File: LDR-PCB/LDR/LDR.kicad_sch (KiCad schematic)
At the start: 7 parts, among them J1 Conn_01x03_Socket, Q1 NPN, U1 ${SIM.PARAMS}

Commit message: merge
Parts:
- added H1, H2: MountingHole_Pad, MountingHole:MountingHole_2.2mm_M2_ISO14580_Pad, symbol Mechanical:MountingHole_Pad
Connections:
- net GND: now also H1.1, H2.1
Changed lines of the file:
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@@
+    (stroke (width 0) (type default))
+  )
+  (wire (pts (xy 96.52 73.025) (xy 96.52 74.93))
     (stroke (width 0) (type default))
   )
@@
   )
   (wire (pts (xy 150.495 85.09) (xy 151.13 85.09))
+    (stroke (width 0) (type default))
+  )
+  (wire (pts (xy 88.265 73.025) (xy 88.265 74.295))
     (stroke (width 0) (type default))
   )
@@
     )
   )
+  (symbol (lib_id "power:GND") (at 88.265 74.295 0) (unit 1)
+    (in_bom yes) (on_board yes) (dnp no) (fields_autoplaced)
+    (property "Reference" "#PWR010" (at 88.265 80.645 0)
+      (effects (font (size 1.27 1.27)) hide)
+    )
+    (property "Value" "GND" (at 88.265 79.375 0)
+      (effects (font (size 1.27 1.27)) hide)
+    )
+    (property "Footprint" "" (at 88.265 74.295 0)
+      (effects (font (size 1.27 1.27)) hide)
+    )
+    (property "Datasheet" "" (at 88.265 74.295 0)
+      (effects (font (size 1.27 1.27)) hide)
+    )
+    (pin "1")
+    (instances
+      (project "LDR"
+        (path "/2e6b5c95-f01c-4aeb-aaa9-5aa7ab28cad0"
+          (reference "#PWR010") (unit 1)
+        )
+      )
+    )
+  )
   (symbol (lib_id "Device:R") (at 138.43 97.79 90) (unit 1)
     (in_bom yes) (on_board yes) (dnp no) (fields_autoplaced)
@@
       (effects (font (size 1.27 1.27)) hide)
     )
+    (pin "1")
+    (pin "2")
     (pin "3")
-    (pin "2")
-    (pin "1")
+    (pin "4")
     (pin "8")
-    (pin "4")
     (instances
       (project "LDR"
@@
     )
   )
+  (symbol (lib_id "power:GND") (at 96.52 74.93 0) (unit 1)
+    (in_bom yes) (on_board yes) (dnp no) (fields_autoplaced)
+    (property "Reference" "#PWR011" (at 96.52 81.28 0)
+      (effects (font (size 1.27 1.27)) hide)
+    )
+    (property "Value" "GND" (at 96.52 80.01 0)
+      (effects (font (size 1.27 1.27)) hide)
+    )
+    (property "Footprint" "" (at 96.52 74.93 0)
+      (effects (font (size 1.27 1.27)) hide)
+    )
+    (property "Datasheet" "" (at 96.52 74.93 0)
+      (effects (font (size 1.27 1.27)) hide)
+    )
+    (pin "1")
+    (instances
+      (project "LDR"
+        (path "/2e6b5c95-f01c-4aeb-aaa9-5aa7ab28cad0"
+          (reference "#PWR011") (unit 1)
+        )
+      )
+    )
+  )
   (symbol (lib_id "power:GND") (at 151.13 93.98 0) (unit 1)
     (in_bom yes) (on_board yes) (dnp no) (fields_autoplaced)
@@
     )
   )
+  (symbol (lib_id "Mechanical:MountingHole_Pad") (at 96.52 70.485 0) (unit 1)
+    (in_bom yes) (on_board yes) (dnp no) (fields_autoplaced)
+    (property "Reference" "H2" (at 99.695 67.945 0)
+      (effects (font (size 1.27 1.27)) (justify left))
+    )
+    (property "Value" "MountingHole_Pad" (at 99.695 70.485 0)
+      (effects (font (size 1.27 1.27)) (justify left) hide)
+    )
+    (property "Footprint" "MountingHole:MountingHole_2.2mm_M2_ISO14580_Pad" (at 96.52 70.485 0)
+      (effects (font (size 1.27 1.27)) hide)
+    )
+    (property "Datasheet" "~" (at 96.52 70.485 0)
+      (effects (font (size 1.27 1.27)) hide)
+    )
+    (pin "1")
+    (instances
+      (project "LDR"
+        (path "/2e6b5c95-f01c-4aeb-aaa9-5aa7ab28cad0"
+          (reference "H2") (unit 1)
+        )
+      )
+    )
+  )
   (symbol (lib_id "Device:R") (at 151.13 88.9 0) (unit 1)
     (in_bom yes) (on_board yes) (dnp no) (fields_autoplaced)
@@
         )
       )
+    )
+  )
+  (symbol (lib_id "Mechanical:MountingHole_Pad") (at 88.265 70.485 0) (unit 1)
+    (in_bom yes) (on_board yes) (dnp no) (fields_autoplaced)
+    (property "Reference" "H1" (at 91.44 67.945 0)
+      (effects (font (size 1.27 1.27)) (justify left))
+    )
+    (property "Value" "MountingHole_Pad" (at 91.44 70.485 0)
+      (effects (font (size 1.27 1.27)) (justify left) hide)
+    )
+    (property "Footprint" "MountingHole:MountingHole_2.2mm_M2_ISO14580_Pad" (at 88.265 70.485 0)
+      (effects (font (size 1.27 1.27)) hide)
+    )
+    (property "Datasheet" "~" (at 88.265 70.485 0)
+      (effects (font (size 1.27 1.27)) hide)
+    )
+    (pin "1")
+    (instances
+      (project "LDR"
+        (path "/2e6b5c95-f01c-4aeb-aaa9-5aa7ab28cad0"
+          (reference "H1") (unit 1)
+        )
+      )

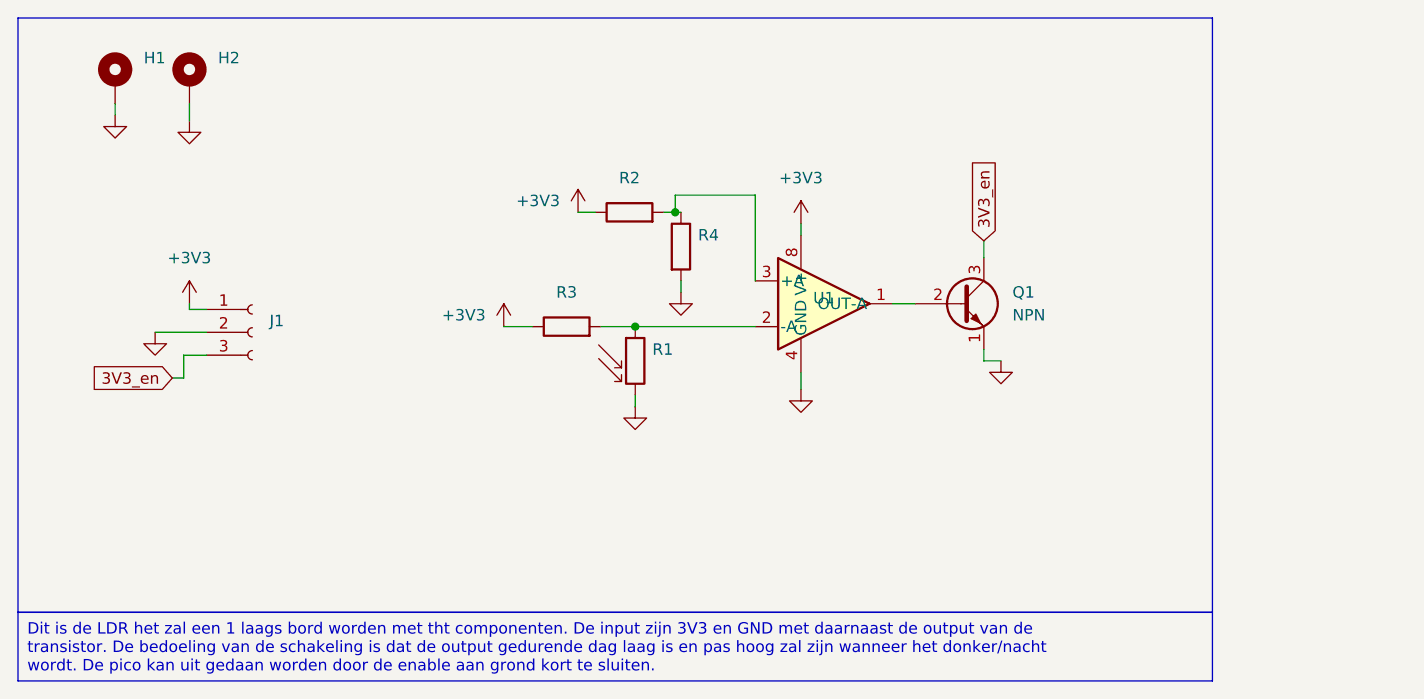
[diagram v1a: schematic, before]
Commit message: LDR schakeling update naar LM311P
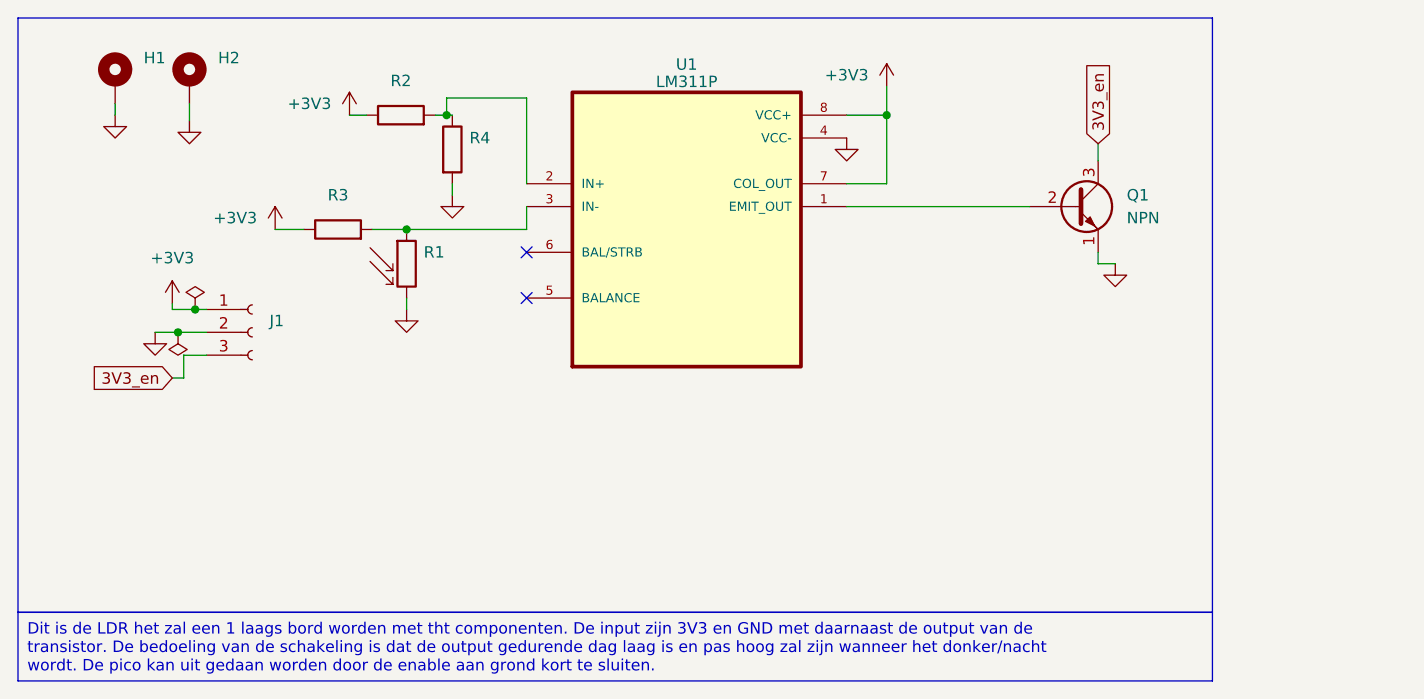
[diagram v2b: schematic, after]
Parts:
- removed U1: ${SIM.PARAMS}, Package_DIP:DIP-8_W7.62mm, symbol Simulation_SPICE:OPAMP
- added U1: LM311P, LM311P:DIP794W45P254L959H508Q8, symbol LM311P:LM311P
- R2, R3: value R -> 2K2
- R4: value R -> 1K8
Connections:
- net +3V3: now also U1.7 (COL_OUT), U1.8 (VCC+)
- net GND: now also U1.4 (VCC-)
- net at R1.1, R3.2: now also U1.3 (IN-)
- net at Q1.2 (B): now also U1.1 (EMIT_OUT)
- net at R2.2, R4.1: now also U1.2 (IN+)
- no-connect marks 0 -> 2
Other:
- moved on the sheet: Q1, R1, R2, R3, R4

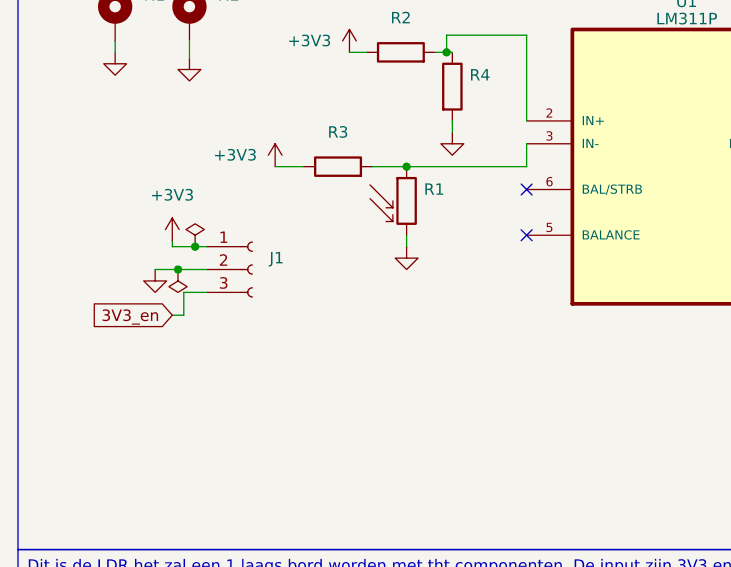
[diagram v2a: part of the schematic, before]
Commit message: LDR connector, silkscreen AC,  Mounting hole main pcb aangepast
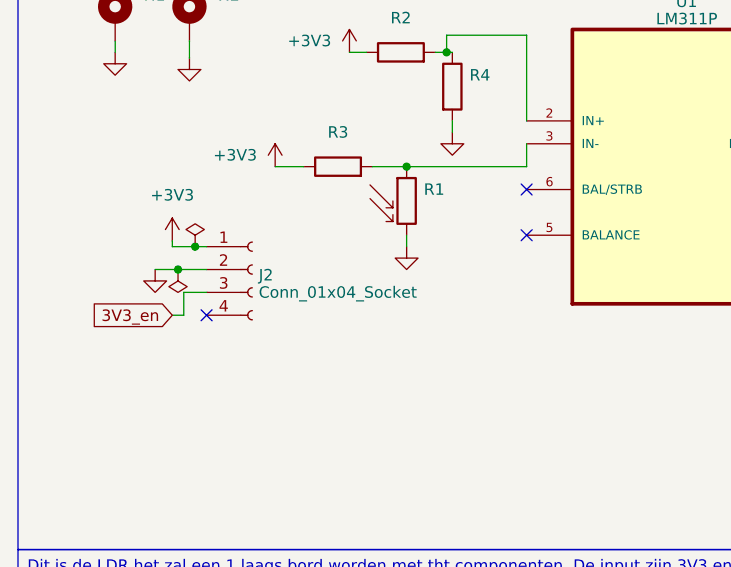
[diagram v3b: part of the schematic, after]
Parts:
- removed J1: Conn_01x03_Socket, Connector_PinSocket_2.00mm:PinSocket_1x03_P2.00mm_Vertical, symbol Connector:Conn_01x03_Socket
- added J2: Conn_01x04_Socket, Connector_JST:JST_EH_B4B-EH-A_1x04_P2.50mm_Vertical, symbol Connector:Conn_01x04_Socket
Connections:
- net +3V3: now also J2.1 (Pin_1)
- net 3V3_en: now also J2.3 (Pin_3)
- net GND: now also J2.2 (Pin_2)
- no-connect marks 2 -> 3
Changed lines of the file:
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@@
   (junction (at 97.155 95.885) (diameter 0) (color 0 0 0 0)
   )
+  (no_connect (at 98.425 103.505))
   (no_connect (at 133.985 89.535))
   (no_connect (at 133.985 94.615))
@@
     )
   )
-  (symbol (lib_id "power:GND") (at 199.39 90.805 0) (unit 1)
-    (in_bom yes) (on_board yes) (dnp no) (fields_autoplaced)
-    (property "Reference" "#PWR07" (at 199.39 97.155 0)
-      (effects (font (size 1.27 1.27)) hide)
-    )
-    (property "Value" "GND" (at 199.39 95.885 0)
-      (effects (font (size 1.27 1.27)) hide)
-    )
-    (property "Footprint" "" (at 199.39 90.805 0)
-      (effects (font (size 1.27 1.27)) hide)
-    )
-    (property "Datasheet" "" (at 199.39 90.805 0)
-      (effects (font (size 1.27 1.27)) hide)
-    )
-    (pin "1")
-    (instances
-      (project "LDR"
-        (path "/2e6b5c95-f01c-4aeb-aaa9-5aa7ab28cad0"
-          (reference "#PWR07") (unit 1)
-        )
-      )
-    )
-  )
-  (symbol (lib_id "Connector:Conn_01x03_Socket") (at 103.505 98.425 0) (unit 1)
-    (in_bom yes) (on_board yes) (dnp no) (fields_autoplaced)
-    (property "Reference" "J1" (at 105.41 97.155 0)
+  (symbol (lib_id "Connector:Conn_01x04_Socket") (at 103.505 98.425 0) (unit 1)
+    (in_bom yes) (on_board yes) (dnp no) (fields_autoplaced)
+    (property "Reference" "J2" (at 104.2162 99.0513 0)
       (effects (font (size 1.27 1.27)) (justify left))
     )
-    (property "Value" "Conn_01x03_Socket" (at 105.41 99.695 0)
-      (effects (font (size 1.27 1.27)) (justify left) hide)
-    )
-    (property "Footprint" "Connector_PinSocket_2.00mm:PinSocket_1x03_P2.00mm_Vertical" (at 103.505 98.425 0)
+    (property "Value" "Conn_01x04_Socket" (at 104.2162 100.9723 0)
+      (effects (font (size 1.27 1.27)) (justify left))
+    )
+    (property "Footprint" "Connector_JST:JST_EH_B4B-EH-A_1x04_P2.50mm_Vertical" (at 103.505 98.425 0)
       (effects (font (size 1.27 1.27)) hide)
     )
@@
     (pin "2")
     (pin "3")
-    (instances
-      (project "LDR"
-        (path "/2e6b5c95-f01c-4aeb-aaa9-5aa7ab28cad0"
-          (reference "J1") (unit 1)
-        )
-      )
+    (pin "4")
+    (instances
+      (project "LDR"
+        (path "/2e6b5c95-f01c-4aeb-aaa9-5aa7ab28cad0"
+          (reference "J2") (unit 1)
+        )
+      )
+    )
+  )
+  (symbol (lib_id "power:GND") (at 199.39 90.805 0) (unit 1)
+    (in_bom yes) (on_board yes) (dnp no) (fields_autoplaced)
+    (property "Reference" "#PWR07" (at 199.39 97.155 0)
+      (effects (font (size 1.27 1.27)) hide)
+    )
+    (property "Value" "GND" (at 199.39 95.885 0)
+      (effects (font (size 1.27 1.27)) hide)
+    )
+    (property "Footprint" "" (at 199.39 90.805 0)
+      (effects (font (size 1.27 1.27)) hide)
+    )
+    (property "Datasheet" "" (at 199.39 90.805 0)
+      (effects (font (size 1.27 1.27)) hide)
+    )
+    (pin "1")
+    (instances
+      (project "LDR"
+        (path "/2e6b5c95-f01c-4aeb-aaa9-5aa7ab28cad0"
+          (reference "#PWR07") (unit 1)
+        )
+      )
